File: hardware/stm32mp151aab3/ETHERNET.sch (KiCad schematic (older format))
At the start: 24 parts

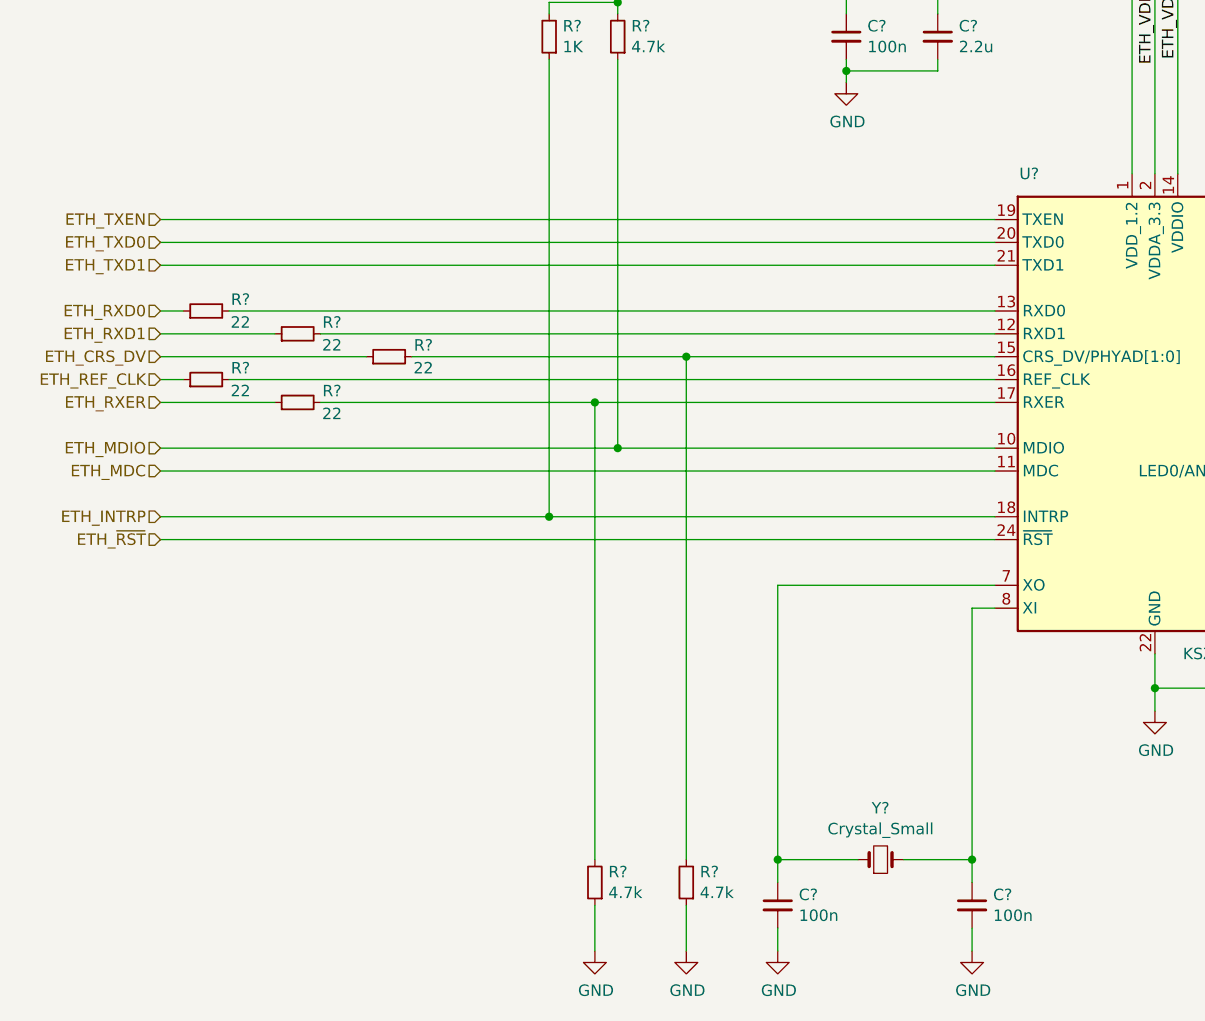
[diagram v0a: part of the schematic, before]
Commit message: update schematic and pdf
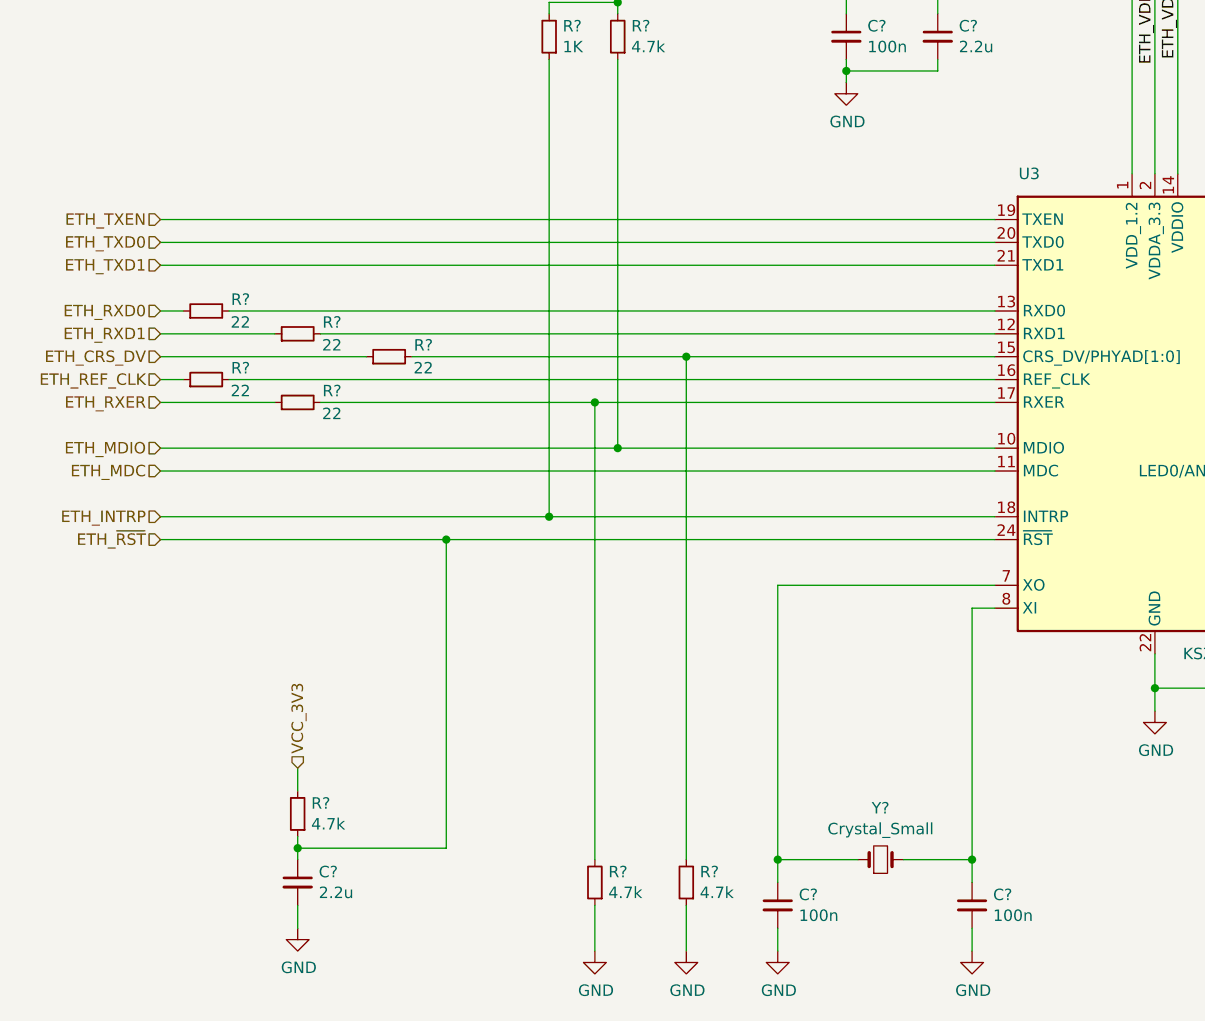
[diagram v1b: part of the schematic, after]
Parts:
- added C?: 2.2u, Capacitor_SMD:C_0805_2012Metric, symbol Device:C_Small
- added R?: 4.7k, Resistor_SMD:R_0805_2012Metric, symbol Device:R_Small
- gave numbers to parts that had none: 1
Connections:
- net ETH_~RST: now also C?.1, R?.1
- net GND: now also C?.2
- net VCC_3V3: now also R?.2
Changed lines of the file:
@@
 $Descr A4 11693 8268
 encoding utf-8
-Sheet 7 7
+Sheet 6 7
 Title ""
 Date ""
@@
 VCC_3V3
 $Comp
-L Interface_Ethernet:KSZ8081RNA U?
+L Interface_Ethernet:KSZ8081RNA U3
 U 1 1 601756AE
 P 5900 4600
-F 0 "U?" H 5350 5700 50  0000 C CNN
+F 0 "U3" H 5350 5700 50  0000 C CNN
 F 1 "KSZ8081RNA" H 6250 3600 50  0000 C CNN
 F 2 "Package_DFN_QFN:QFN-24-1EP_4x4mm_P0.5mm_EP2.6x2.6mm" H 7300 3600 50  0001 C CNN
@@
 ETH_~RST
 Wire Wire Line
-	5200 5100 1550 5100
+	5200 5100 2800 5100
 Text Label 5900 2650 3    50   ~ 0
 ETH_VDDA
+$Comp
+L Device:C_Small C?
+U 1 1 60EE2F12
+P 2150 6600
+F 0 "C?" H 2242 6646 50  0000 L CNN
+F 1 "2.2u" H 2242 6555 50  0000 L CNN
+F 2 "Capacitor_SMD:C_0805_2012Metric" H 2150 6600 50  0001 C CNN
+F 3 "~" H 2150 6600 50  0001 C CNN
+	1    2150 6600
+	1    0    0    -1
+$EndComp
+$Comp
+L Device:R_Small R?
+U 1 1 60EE48B2
+P 2150 6300
+F 0 "R?" H 2091 6254 50  0000 R CNN
+F 1 "4.7k" H 2091 6345 50  0000 R CNN
+F 2 "Resistor_SMD:R_0805_2012Metric" H 2150 6300 50  0001 C CNN
+F 3 "~" H 2150 6300 50  0001 C CNN
+	1    2150 6300
+	-1   0    0    1
+$EndComp
+Wire Wire Line
+	2150 6400 2150 6450
+Wire Wire Line
+	2150 6450 2800 6450
+Wire Wire Line
+	2800 6450 2800 5100
+Connection ~ 2150 6450
+Wire Wire Line
+	2150 6450 2150 6500
+Connection ~ 2800 5100
+Wire Wire Line
+	2800 5100 1550 5100
+Text HLabel 2150 6100 1    50   Input ~ 0
+VCC_3V3
+Wire Wire Line
+	2150 6100 2150 6200
+$Comp
+L power:GND #PWR?
+U 1 1 60EEF3AB
+P 2150 6800
+F 0 "#PWR?" H 2150 6550 50  0001 C CNN
+F 1 "GND" H 2155 6627 50  0000 C CNN
+F 2 "" H 2150 6800 50  0001 C CNN
+F 3 "" H 2150 6800 50  0001 C CNN
+	1    2150 6800
+	1    0    0    -1
+$EndComp
+Wire Wire Line
+	2150 6700 2150 6800
 $EndSCHEMATC
